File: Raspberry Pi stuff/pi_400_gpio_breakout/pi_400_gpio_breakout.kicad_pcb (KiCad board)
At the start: 4 copper layers, 65.2 x 61.4 mm, 14 parts, among them J1 I2C, J2 RPI_IN, J3 SPI_I2S, J4 QWIIC1, J5 RPI_IN, J5 Raspberry_Pi_2_3, J6 QWIIC2

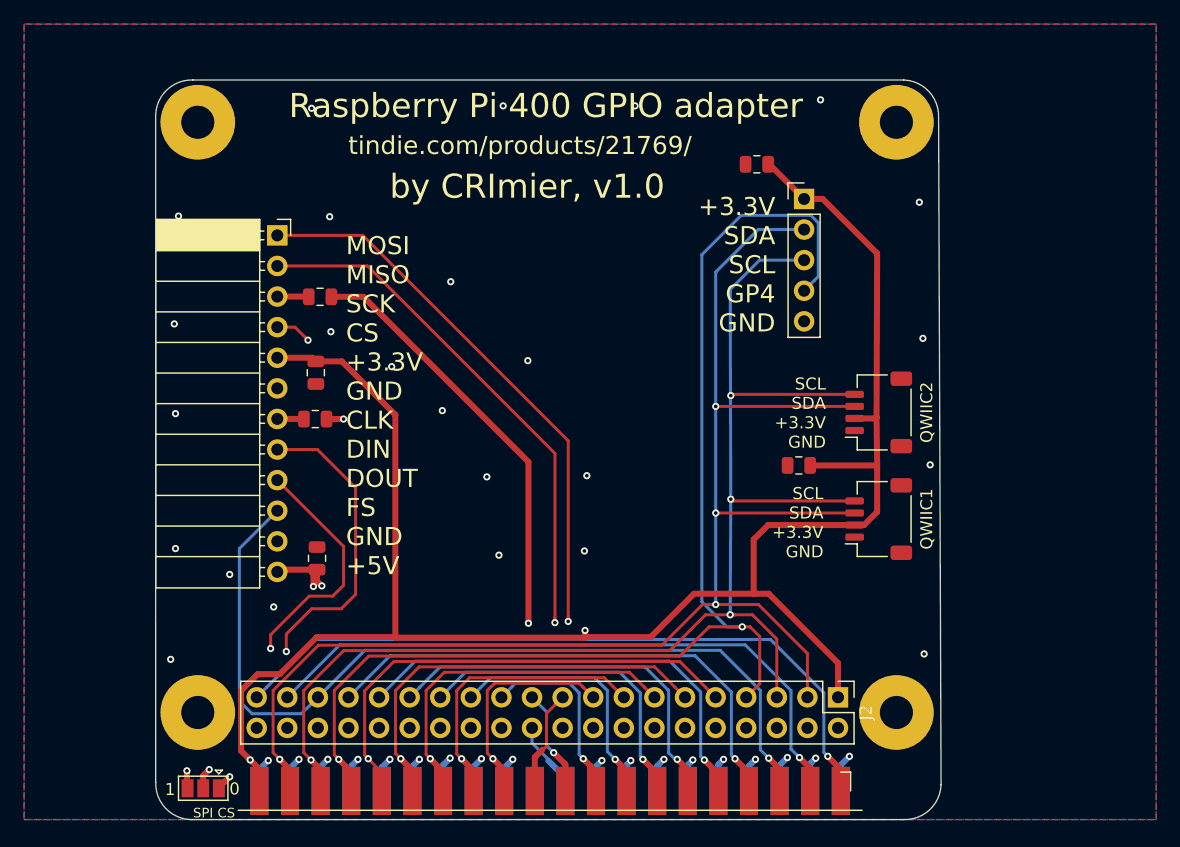
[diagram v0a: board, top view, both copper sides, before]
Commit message: Pi 400 GPIO breakout v2. Adding this in part because I'll try to re-route it now and might fail at that, so will need to fall back to the previous version.
Force pushed later on  - forgot to regenerate zones.
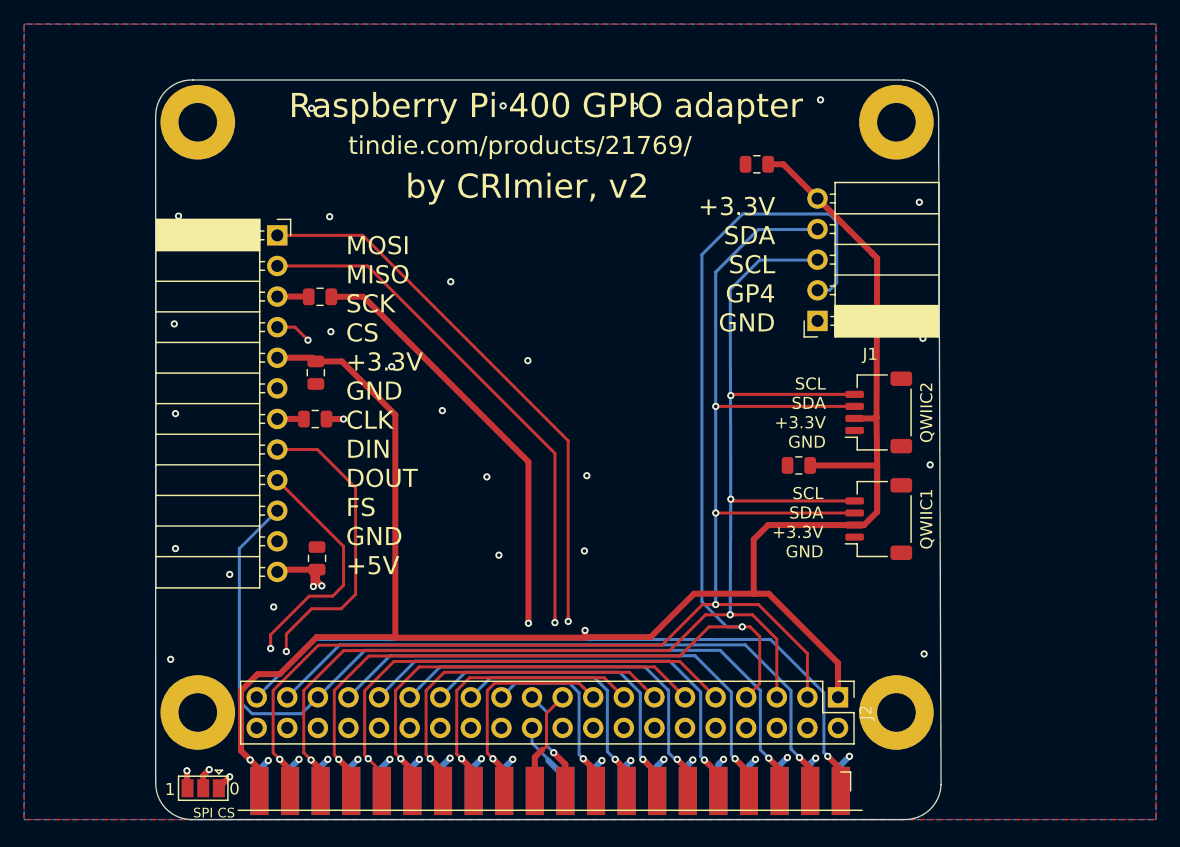
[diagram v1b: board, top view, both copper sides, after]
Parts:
- J1: footprint Connector_PinHeader_2.54mm:PinHeader_1x05_P2.54mm_Vertical -> Connector_PinSocket_2.54mm:PinSocket_1x05_P2.54mm_Horizontal
- moved J1 10.2 mm to (185.2, 85.6), turned to 180 degrees
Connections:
- J1 pad 1: +3V3 -> GND
- J1 pad 2: /SDA -> /GP4
- J1 pad 4: /GP4 -> /SDA
- J1 pad 5: GND -> +3V3
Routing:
- net /GP4: track 102.7 -> 105.2 mm
- net /SCL: track 111.7 -> 112.8 mm
- net /SDA: track 123.1 -> 124.2 mm
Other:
- board text added: "by CRImier, v2"
- board text removed: "by CRImier, v1.0"
